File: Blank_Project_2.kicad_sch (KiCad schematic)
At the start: 6 parts

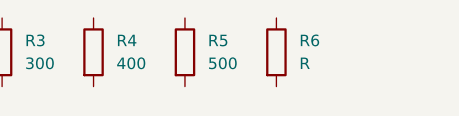
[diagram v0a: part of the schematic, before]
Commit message: Added a resistor.
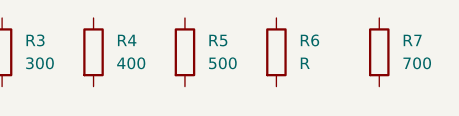
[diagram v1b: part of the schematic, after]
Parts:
- added R7: 700, symbol Device:R
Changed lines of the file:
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@@
+    )
+  )
+  (symbol (lib_id "Device:R") (at 138.43 86.36 0) (unit 1)
+    (in_bom yes) (on_board yes) (dnp no) (fields_autoplaced)
+    (property "Reference" "R7" (at 140.97 85.09 0)
+      (effects (font (size 1.27 1.27)) (justify left))
+    )
+    (property "Value" "700" (at 140.97 87.63 0)
+      (effects (font (size 1.27 1.27)) (justify left))
+    )
+    (property "Footprint" "" (at 136.652 86.36 90)
+      (effects (font (size 1.27 1.27)) hide)
+    )
+    (property "Datasheet" "~" (at 138.43 86.36 0)
+      (effects (font (size 1.27 1.27)) hide)
+    )
+    (property "Purpose" "" (at 138.43 86.36 0)
+      (effects (font (size 1.27 1.27)))
+    )
+    (pin "1")
+    (pin "2")
+    (instances
+      (project "Blank_Project_2"
+        (path "/5b8242ae-0f09-4121-9be1-acd0eee8c5c7"
+          (reference "R7") (unit 1)
+        )
+      )
     )
   )

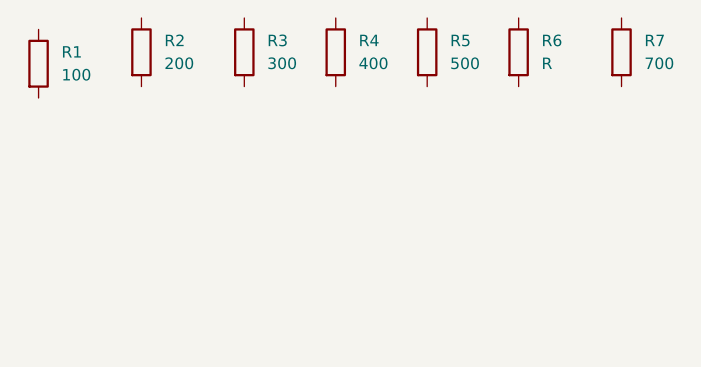
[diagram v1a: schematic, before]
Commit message: Added capacitor, C1
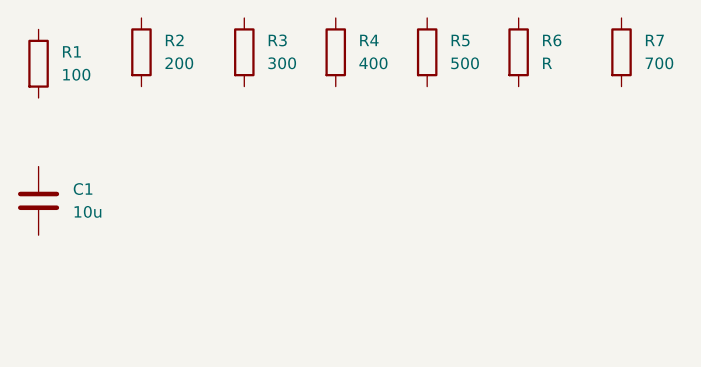
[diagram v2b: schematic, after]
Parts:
- added C1: 10u, symbol Device:C
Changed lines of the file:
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@@
+    )
+  )
+  (symbol (lib_id "Device:C") (at 73.66 102.87 0) (unit 1)
+    (in_bom yes) (on_board yes) (dnp no) (fields_autoplaced)
+    (property "Reference" "C1" (at 77.47 101.6 0)
+      (effects (font (size 1.27 1.27)) (justify left))
+    )
+    (property "Value" "10u" (at 77.47 104.14 0)
+      (effects (font (size 1.27 1.27)) (justify left))
+    )
+    (property "Footprint" "" (at 74.6252 106.68 0)
+      (effects (font (size 1.27 1.27)) hide)
+    )
+    (property "Datasheet" "~" (at 73.66 102.87 0)
+      (effects (font (size 1.27 1.27)) hide)
+    )
+    (property "Purpose" "" (at 73.66 102.87 0)
+      (effects (font (size 1.27 1.27)))
+    )
+    (pin "1")
+    (pin "2")
+    (instances
+      (project "Blank_Project_2"
+        (path "/5b8242ae-0f09-4121-9be1-acd0eee8c5c7"
+          (reference "C1") (unit 1)
+        )
+      )
     )
   )

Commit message: Added R8
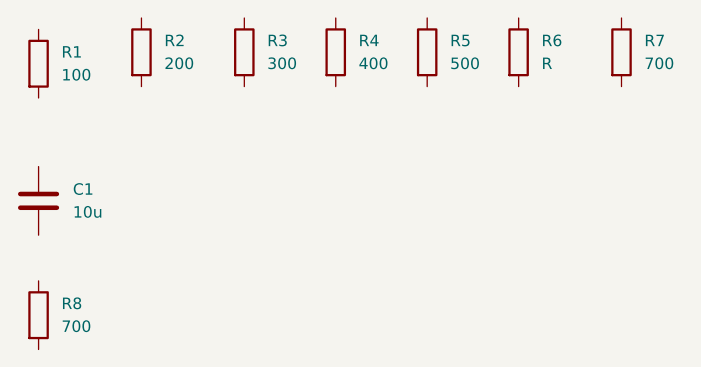
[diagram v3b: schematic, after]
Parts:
- added R8: 700, symbol Device:R
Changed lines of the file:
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@@
+    )
+  )
+  (symbol (lib_id "Device:R") (at 73.66 115.57 0) (unit 1)
+    (in_bom yes) (on_board yes) (dnp no) (fields_autoplaced)
+    (property "Reference" "R8" (at 76.2 114.3 0)
+      (effects (font (size 1.27 1.27)) (justify left))
+    )
+    (property "Value" "700" (at 76.2 116.84 0)
+      (effects (font (size 1.27 1.27)) (justify left))
+    )
+    (property "Footprint" "" (at 71.882 115.57 90)
+      (effects (font (size 1.27 1.27)) hide)
+    )
+    (property "Datasheet" "~" (at 73.66 115.57 0)
+      (effects (font (size 1.27 1.27)) hide)
+    )
+    (property "Purpose" "" (at 73.66 115.57 0)
+      (effects (font (size 1.27 1.27)))
+    )
+    (pin "1")
+    (pin "2")
+    (instances
+      (project "Blank_Project_2"
+        (path "/5b8242ae-0f09-4121-9be1-acd0eee8c5c7"
+          (reference "R8") (unit 1)
+        )
+      )
     )
   )
